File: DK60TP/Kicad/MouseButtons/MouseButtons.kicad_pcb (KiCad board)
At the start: 2 copper layers, 78.2 x 19 mm, 11 parts, among them K1 K43, K2 K43, K3 K44, K4 K45, K5 K45, P1 CONN_01X04

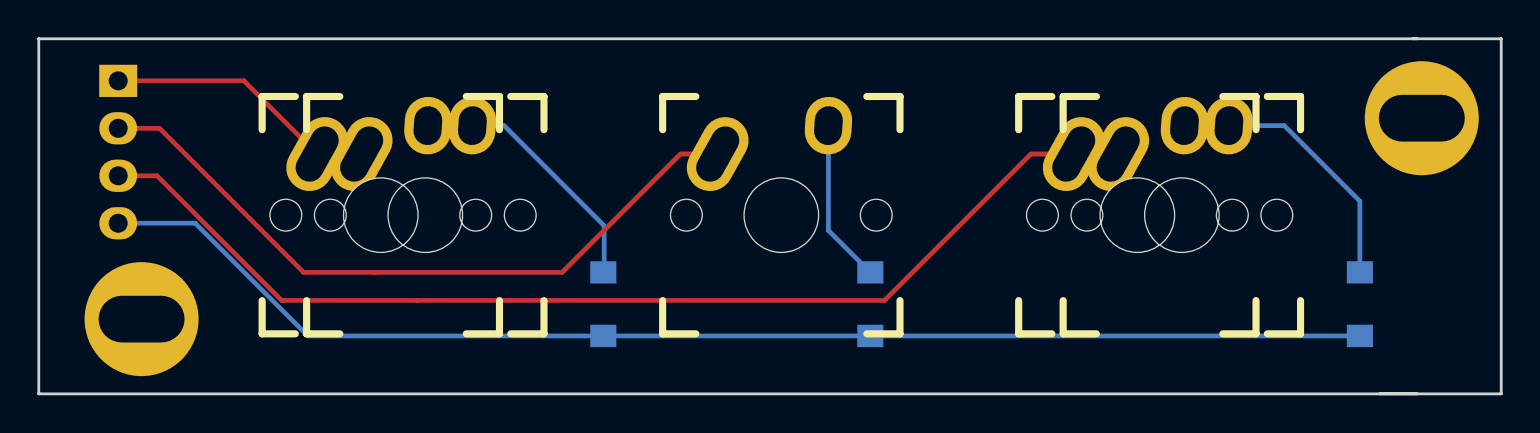
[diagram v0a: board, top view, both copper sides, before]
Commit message: - DK60TP: reducing quantity of VIAs
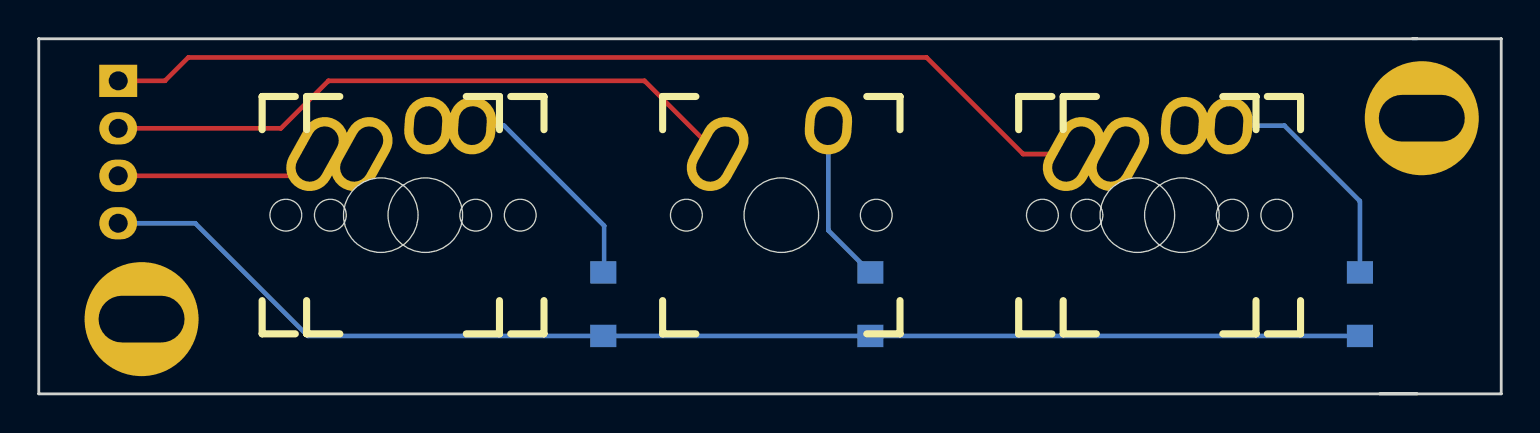
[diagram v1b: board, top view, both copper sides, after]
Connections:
- P1 pad 1: Col3 -> Col5
- P1 pad 3: Col5 -> Col3
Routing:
- net Col5: track 59.5 -> 56.2 mm
- net Col4: track 37.9 -> 34.8 mm
- net Col3: track 15.6 -> 14.5 mm
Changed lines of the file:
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@@
     (links 13)
     (no_connects 0)
-    (area 86.614287 54.55 186.6 87.950001)
+    (area 95.924999 61.924999 174.325001 81.075001)
     (thickness 1.6)
     (drawings 12)
-    (tracks 33)
+    (tracks 30)
     (zones 0)
     (modules 11)
@@
     (fp_line (start 1.524 -3.81) (end 4.064 -3.81) (layer B.SilkS) (width 0.15))
     (pad 1 thru_hole rect (at 0 0 180) (size 2.032 1.7272) (drill 1.016) (layers *.Cu *.Mask)
-      (net 5 Col3))
+      (net 7 Col5))
     (pad 2 thru_hole oval (at 0 -2.54 180) (size 2.032 1.7272) (drill 1.016) (layers *.Cu *.Mask)
       (net 6 Col4))
     (pad 3 thru_hole oval (at 0 -5.08 180) (size 2.032 1.7272) (drill 1.016) (layers *.Cu *.Mask)
-      (net 7 Col5))
+      (net 5 Col3))
     (pad 4 thru_hole oval (at 0 -7.62 180) (size 2.032 1.7272) (drill 1.016) (layers *.Cu *.Mask)
       (net 2 Row4))
@@
   (segment (start 159.6825 66.6475) (end 159.6825 67.9325) (width 0.25) (layer B.Cu) (net 4))
   (segment (start 157.30125 66.6475) (end 159.6825 66.6475) (width 0.25) (layer B.Cu) (net 4))
-  (segment (start 100.25 64.25) (end 106.9775 64.25) (width 0.25) (layer F.Cu) (net 5))
-  (segment (start 106.9775 64.25) (end 110.895 68.1675) (width 0.25) (layer F.Cu) (net 5))
+  (segment (start 100.25 69.33) (end 109.7325 69.33) (width 0.25) (layer F.Cu) (net 5) (status C00000))
+  (segment (start 109.7325 69.33) (end 110.895 68.1675) (width 0.25) (layer F.Cu) (net 5) (status C00000))
   (segment (start 110.2275 67.5) (end 110.895 68.1675) (width 0.25) (layer F.Cu) (net 5))
   (segment (start 110.895 68.1675) (end 113.27625 68.1675) (width 0.25) (layer B.Cu) (net 5))
-  (segment (start 100.25 66.79) (end 102.46 66.79) (width 0.25) (layer F.Cu) (net 6))
-  (segment (start 110.17 74.5) (end 114 74.5) (width 0.25) (layer F.Cu) (net 6))
-  (segment (start 102.46 66.79) (end 110.17 74.5) (width 0.25) (layer F.Cu) (net 6))
-  (segment (start 130.3325 68.1675) (end 132.32625 68.1675) (width 0.25) (layer F.Cu) (net 6))
-  (segment (start 124 74.5) (end 130.3325 68.1675) (width 0.25) (layer F.Cu) (net 6))
-  (segment (start 114 74.5) (end 124 74.5) (width 0.25) (layer F.Cu) (net 6))
-  (segment (start 100.25 69.33) (end 102.33 69.33) (width 0.25) (layer F.Cu) (net 7))
-  (segment (start 109 76) (end 116.25 76) (width 0.25) (layer F.Cu) (net 7))
-  (segment (start 102.33 69.33) (end 109 76) (width 0.25) (layer F.Cu) (net 7))
-  (segment (start 149.0825 68.1675) (end 151.37625 68.1675) (width 0.25) (layer F.Cu) (net 7))
-  (segment (start 141.25 76) (end 149.0825 68.1675) (width 0.25) (layer F.Cu) (net 7))
-  (segment (start 116.25 76) (end 141.25 76) (width 0.25) (layer F.Cu) (net 7))
+  (segment (start 100.25 66.79) (end 108.96 66.79) (width 0.25) (layer F.Cu) (net 6) (status 400000))
+  (segment (start 128.40875 64.25) (end 132.32625 68.1675) (width 0.25) (layer F.Cu) (net 6) (status 800000))
+  (segment (start 111.5 64.25) (end 128.40875 64.25) (width 0.25) (layer F.Cu) (net 6))
+  (segment (start 108.96 66.79) (end 111.5 64.25) (width 0.25) (layer F.Cu) (net 6))
+  (segment (start 151.37625 68.1675) (end 148.6675 68.1675) (width 0.25) (layer F.Cu) (net 7) (status 400000))
+  (segment (start 102.75 64.25) (end 100.25 64.25) (width 0.25) (layer F.Cu) (net 7) (status 800000))
+  (segment (start 104 63) (end 102.75 64.25) (width 0.25) (layer F.Cu) (net 7))
+  (segment (start 143.5 63) (end 104 63) (width 0.25) (layer F.Cu) (net 7))
+  (segment (start 148.6675 68.1675) (end 143.5 63) (width 0.25) (layer F.Cu) (net 7))
   (segment (start 151.37625 68.1675) (end 153.7575 68.1675) (width 0.25) (layer B.Cu) (net 7))
   (zone (net 0) (net_name "") (layer B.Cu) (hatch edge 0.508)
